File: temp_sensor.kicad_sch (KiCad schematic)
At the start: 42 parts, among them J1 Conn_ARM_JTAG_SWD_10, J3 Conn_01x02_Pin, P1 USB_C_Plug_USB2.0, Q1 AO3401A, Q2 AO3400A, SW1 SW_Push, SW2 SW_Push, U1 nRF52840, U2 MCP73831-2-OT, U4 TMP112xxDRL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

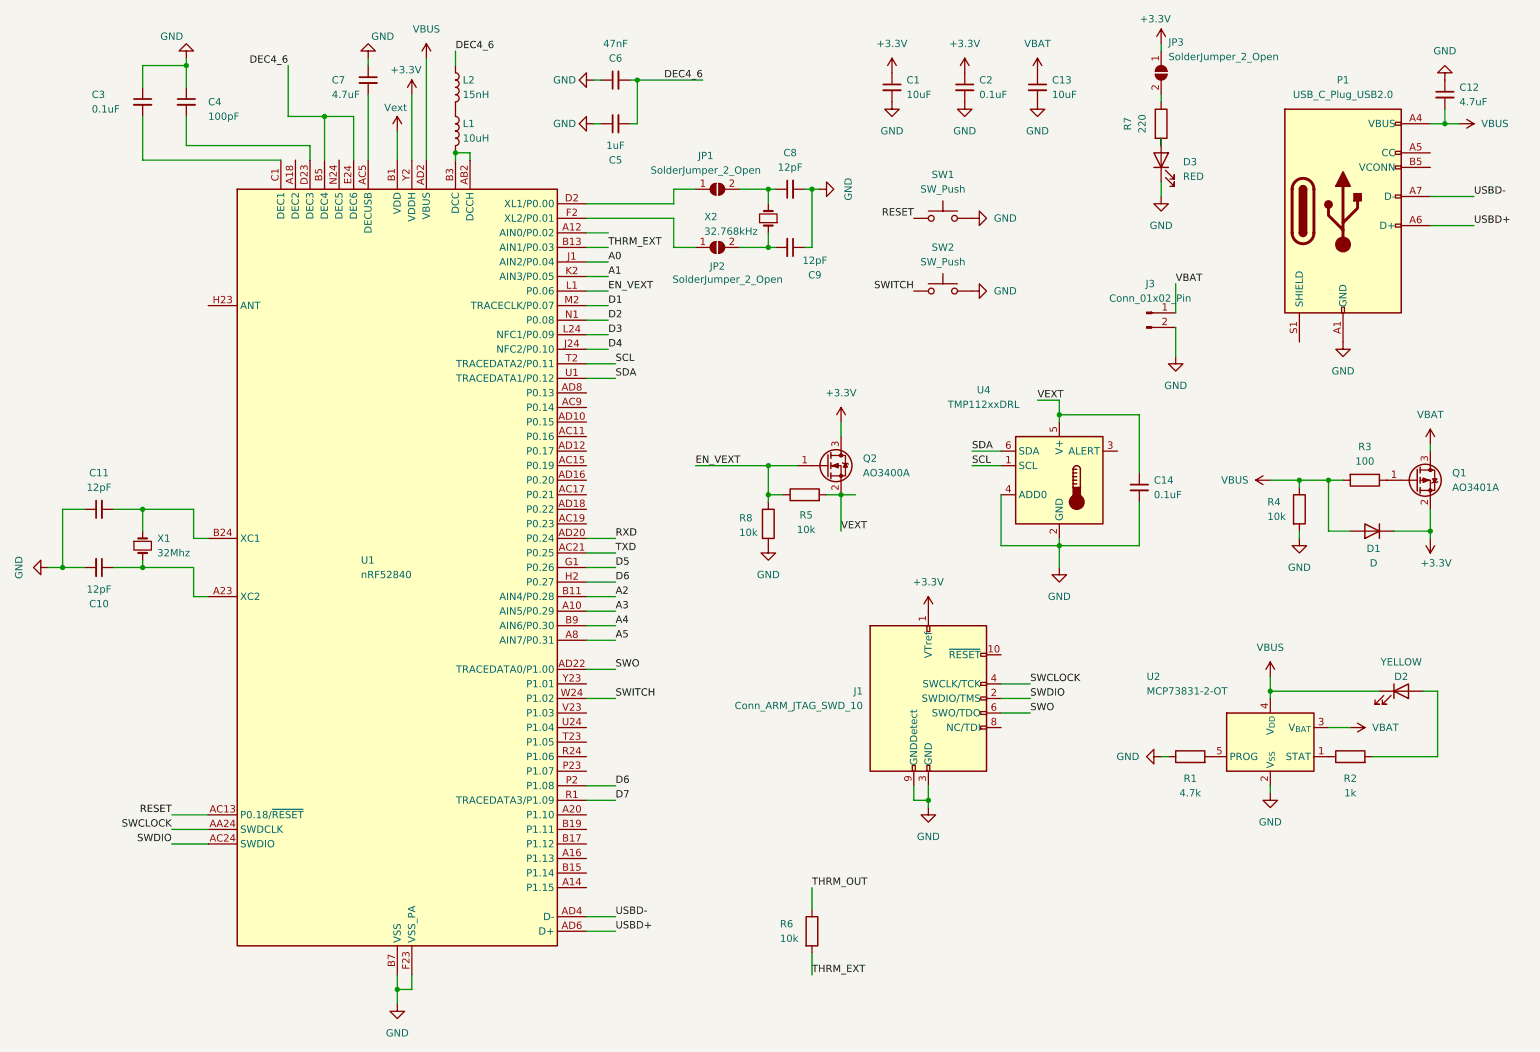
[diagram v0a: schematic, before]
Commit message: Including report generated when added components to PCB
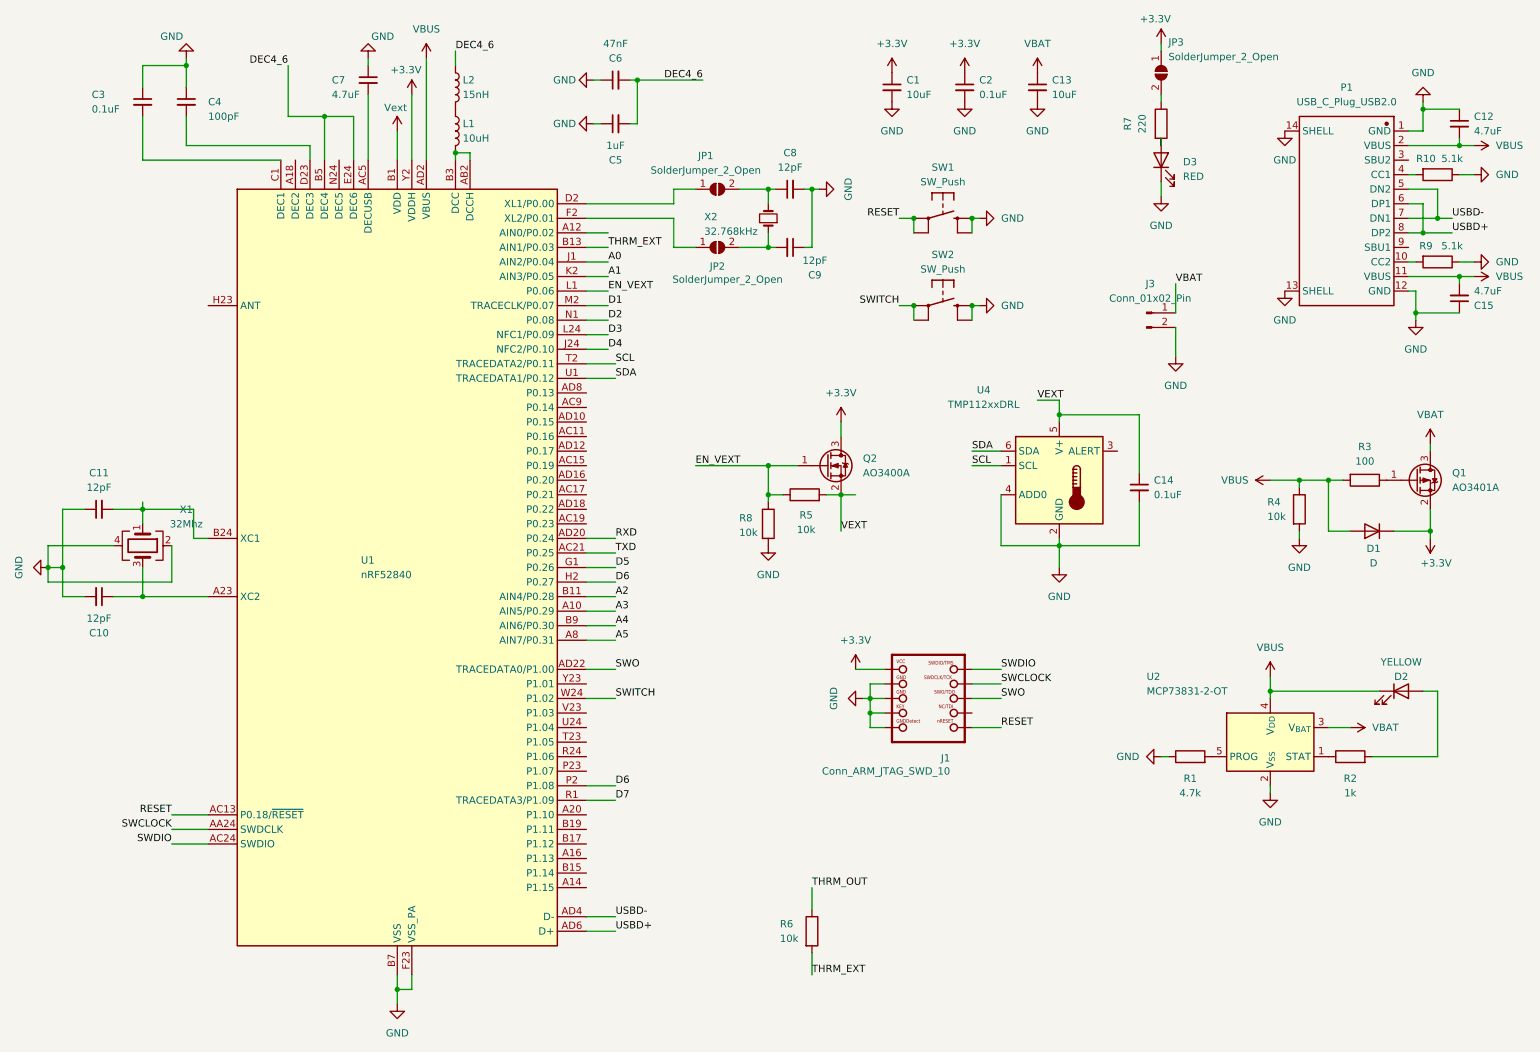
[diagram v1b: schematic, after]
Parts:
- added C15: 4.7uF, custom_jlc_parts:0402_cap, symbol Device:C_Small
- added R10, R9: 5.1k, custom_jlc_parts:0603_res, symbol Device:R
- J1: footprint Adafruit_nRF52840_feather:2X05_1.27MM_BOX_POSTS -> custom_jlc_parts:Adafruit_JTAG_2X05_1.27MM_BOX_POSTS; symbol Connector:Conn_ARM_JTAG_SWD_10 -> Adafruit nRF52840 Bluefruit Feather Express Rev D-eagle-import:JTAG-CORTEXBOXPOSTS
- J3: footprint Adafruit_nRF52840_feather:JSTPH2 -> Connector_JST:JST_PH_S2B-PH-K_1x02_P2.00mm_Horizontal
- P1: footprint custom_jlc_parts:usbc -> custom_jlc_parts:USBC_custom; symbol Connector:USB_C_Plug_USB2.0 -> Custom:USBC 16PIN 2MD(073)
- SW1, SW2: footprint custom_jlc_parts:switch_tactile -> custom_jlc_parts:switch_modify; symbol Switch:SW_Push -> Adafruit nRF52840 Bluefruit Feather Express Rev D-eagle-import:SWITCH_TACT_SMT
- X1: symbol Device:Crystal_Small -> Device:Crystal_GND24
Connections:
- net GND: now also J1.7 (KEY), P1.1 (GND), P1.12 (GND), P1.13 (SHELL), P1.14 (SHELL), SW1.4, SW2.4, X1.2, X1.4, C15.1, R10.1, R9.1; no longer P1.A1 (GND), P1.A12 (GND), P1.B1 (GND), P1.B12 (GND)
- net RESET: now also J1.10 (NRESET), SW1.3
- net SWITCH: now also SW2.3
- net USBD+: now also P1.6 (DP1), P1.8 (DP2); no longer P1.A6 (D+)
- net USBD-: now also P1.5 (DN2), P1.7 (DN1); no longer P1.A7 (D-)
- net VBUS: now also P1.11 (VBUS), P1.2 (VBUS), C15.2; no longer P1.A4 (VBUS), P1.A9 (VBUS), P1.B4 (VBUS), P1.B9 (VBUS)
- net at C10.1, U1.A23 (XC2): now also X1.3; no longer X1.2
- new net: P1.4 (CC1), R10.2
- new net: P1.10 (CC2), R9.2
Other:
- moved on the sheet: C10, C12, J1
